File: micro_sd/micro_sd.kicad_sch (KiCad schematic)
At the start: 0 parts

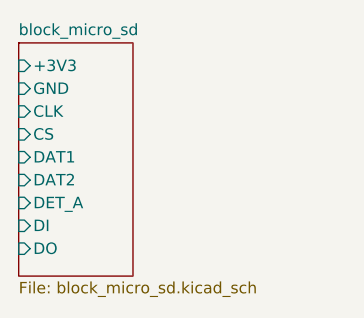
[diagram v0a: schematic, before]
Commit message: fixed microsd
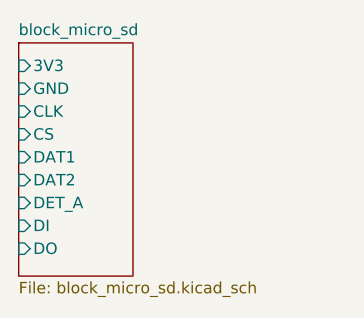
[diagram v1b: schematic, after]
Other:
- sheet block_micro_sd ports: added 3V3; removed +3V3
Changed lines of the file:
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@@
 			)
 		)
-		(pin "+3V3" input
+		(pin "3V3" input
 			(at 114.3 71.12 180)
 			(effects
